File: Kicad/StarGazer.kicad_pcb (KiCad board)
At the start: 4 copper layers, 100 x 100 mm, 102 parts, among them J201 USB_B_Micro, J202 JST - 2x1, J301 JST - 4x1, J302 JST - 4x1, J303 JST - 5x1, J304 JST - 5x1, SW201 JST - 2x1, SW301 RESET PUSH, U101 STM32G070KBT6, U201 STBC08, U202 AP22811BW5-7, U203 TLV75528PDBVR, U301 TSX-3225, U302 LIS3MDLTR, U303 LSM6DS33TR, U304 74HC595PW,112, U305 74HC595PW,112, U306 74HC595PW,112

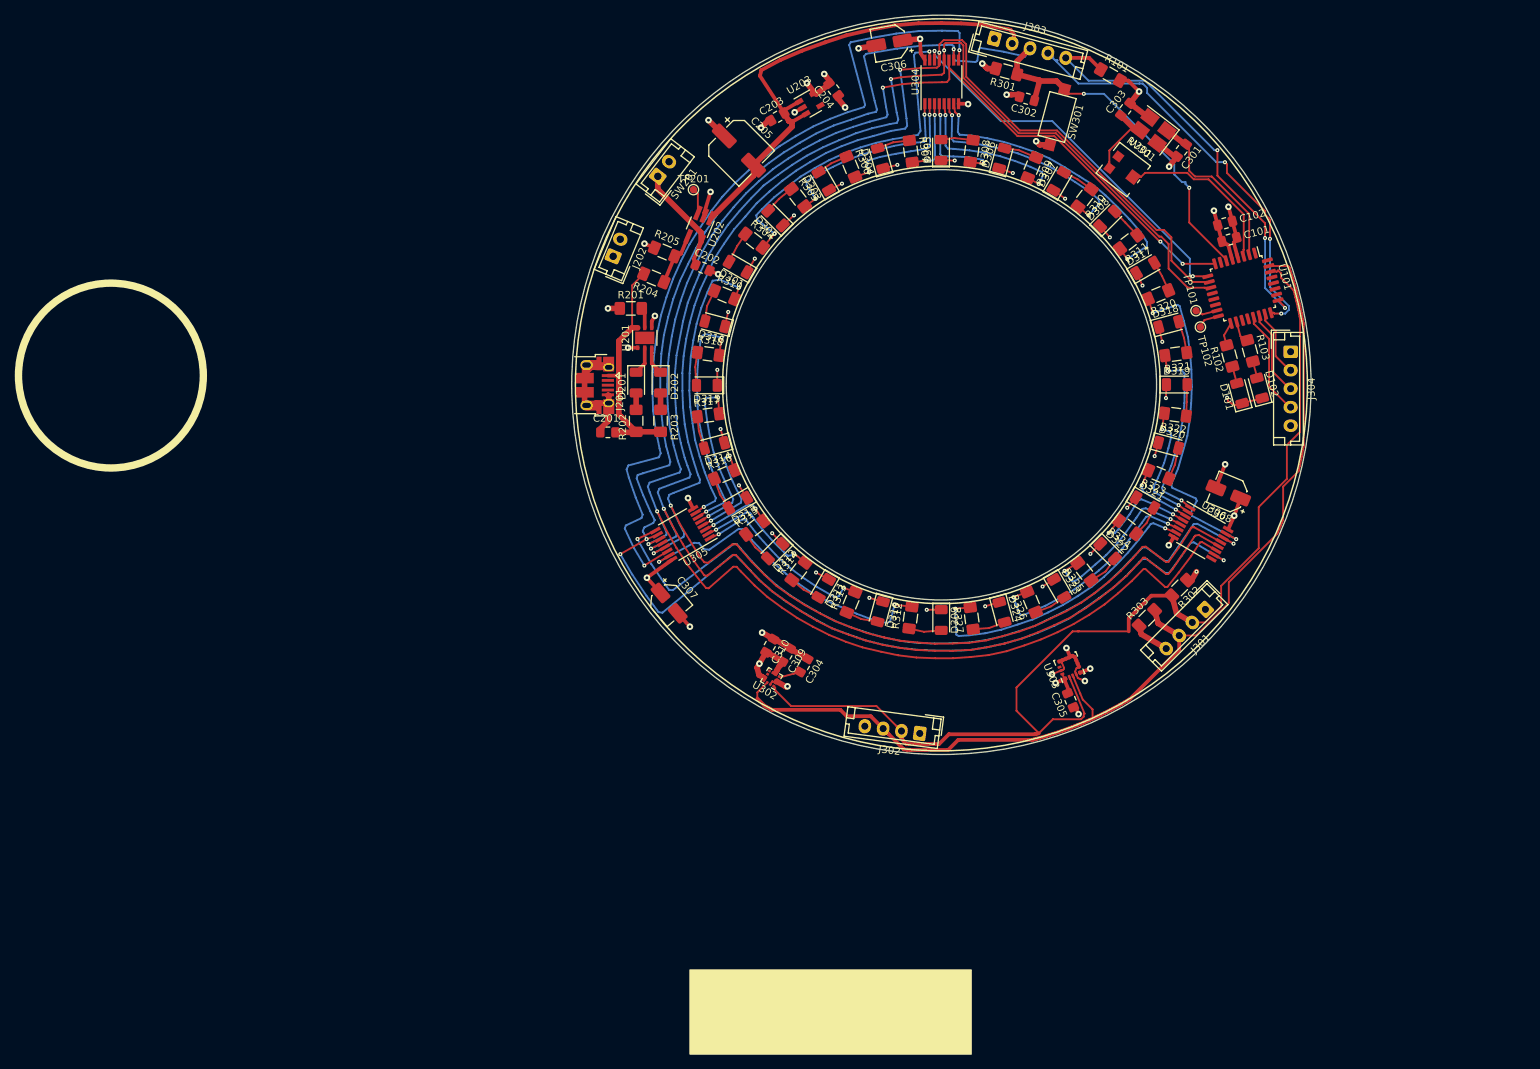
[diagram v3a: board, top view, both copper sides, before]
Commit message: PCB updated to curved traces.  Leftover final polish, screw locations, drill-routing, and art is missing
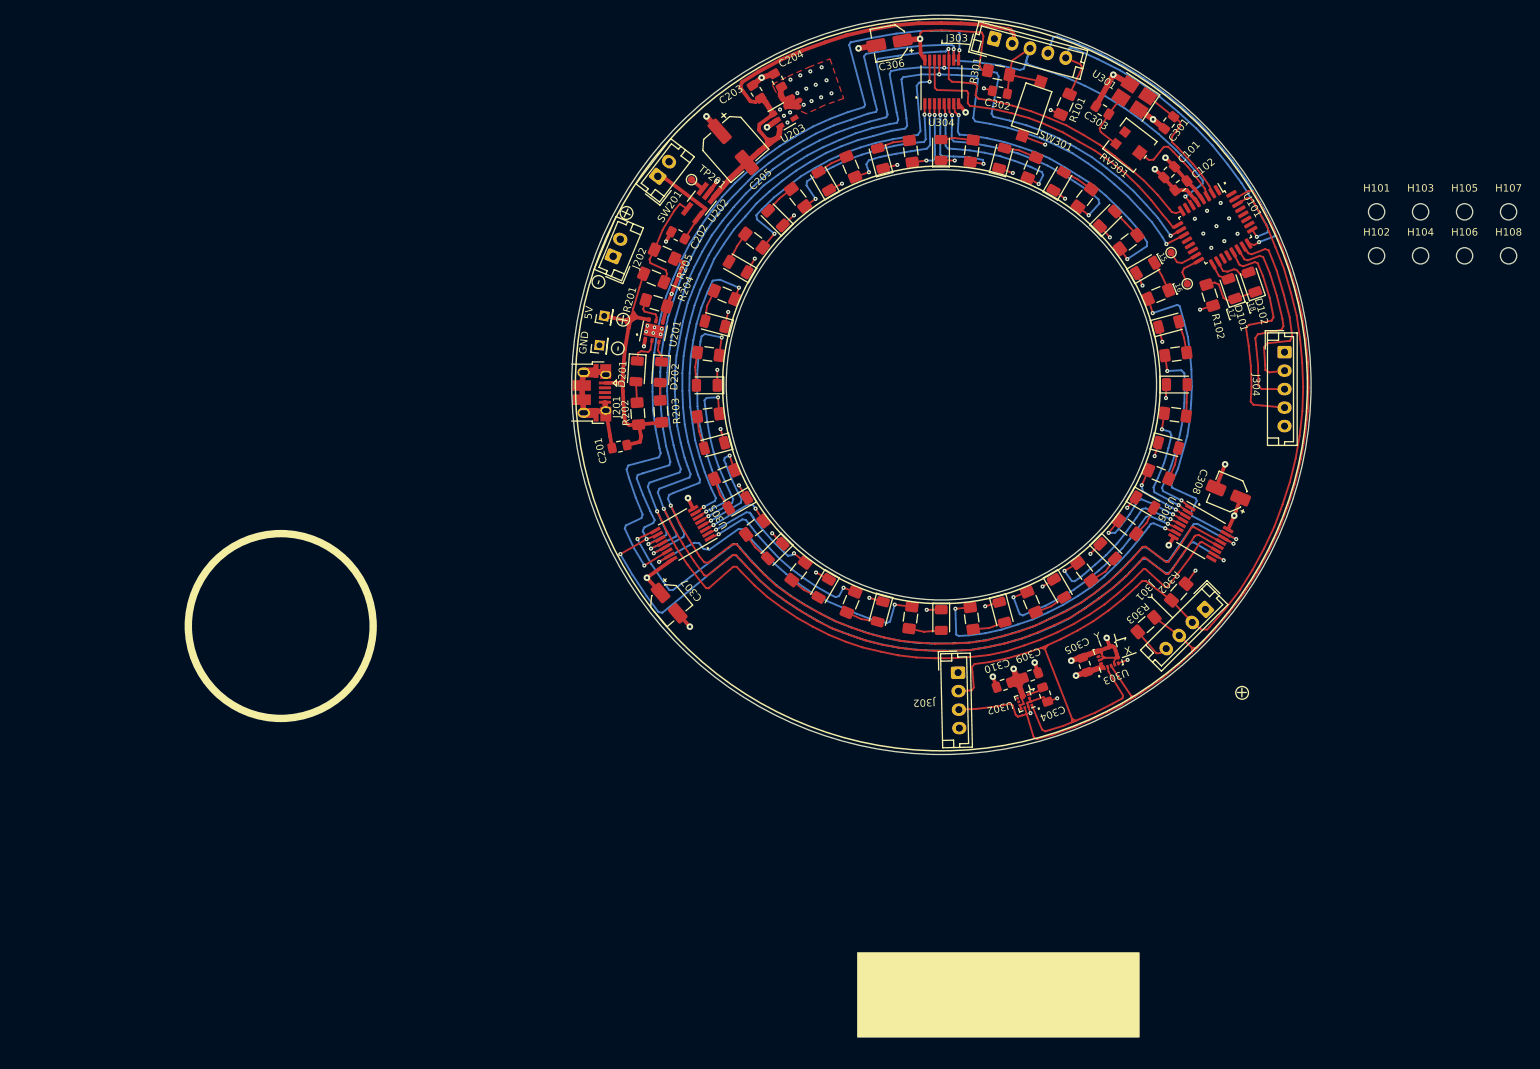
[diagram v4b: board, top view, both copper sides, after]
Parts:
- removed R103: 180ohm, Resistor_SMD:R_1206_3216Metric_Pad1.42x1.75mm_HandSolder
- added H101: MountingHole, MountingHole:MountingHole_2.2mm_M2, F.Cu at (218.8, 66.5)
- added H102: MountingHole, MountingHole:MountingHole_2.2mm_M2, F.Cu at (218.8, 72.5)
- added H103: MountingHole, MountingHole:MountingHole_2.2mm_M2, F.Cu at (224.8, 66.5)
- added H104: MountingHole, MountingHole:MountingHole_2.2mm_M2, F.Cu at (224.8, 72.5)
- added H105: MountingHole, MountingHole:MountingHole_2.2mm_M2, F.Cu at (230.7, 66.5)
- added H106: MountingHole, MountingHole:MountingHole_2.2mm_M2, F.Cu at (230.7, 72.5)
- added H107: MountingHole, MountingHole:MountingHole_2.2mm_M2, F.Cu at (236.7, 66.5)
- added H108: MountingHole, MountingHole:MountingHole_2.2mm_M2, F.Cu at (236.7, 72.5)
- added J203: Conn_01x01, Connector_PinHeader_2.00mm:PinHeader_1x01_P2.00mm_Vertical, F.Cu at (113.7, 84.6)
- added J204: Conn_01x01, Connector_PinHeader_2.00mm:PinHeader_1x01_P2.00mm_Vertical, F.Cu at (114.4, 80.6)
- moved U302 34.4 mm to (171.2, 132.8), turned to 199 degrees
- moved C309 33.2 mm to (172.1, 129.2), turned to 199 degrees
- moved C304 32.9 mm to (174.0, 131.8), turned to 109 degrees
- moved C310 32.1 mm to (168.4, 130.5), turned to 19 degrees
- moved D102 14.4 mm to (202.0, 76.0), turned to 108.8 degrees
- moved D101 14.2 mm to (199.2, 76.9), turned to 108.8 degrees
- moved C101 12.2 mm to (190.8, 61.2), turned to 225.4 degrees
- moved J302 9.71 mm to (162.2, 128.9), turned to 271.3 degrees
- moved U101 9.06 mm to (197.0, 68.6), turned to 300.2 degrees
- moved R102 8.64 mm to (196.3, 77.8), turned to 107.4 degrees
- moved TP101 8.56 mm to (191.0, 72.0)
- moved C102 7.84 mm to (192.4, 63.0), turned to 217.8 degrees
- moved C204 7.65 mm to (137.8, 48.7), turned to 298.5 degrees
- moved R101 7.28 mm to (176.7, 52.0), turned to 246.4 degrees
- moved TP102 6.11 mm to (193.2, 76.3)
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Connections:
- D101 pad 1: GND -> Net-(D101-Pad1)
- D102 pad 1: GND -> Net-(D101-Pad1)
- R102 pad 1: Net-(R102-Pad1) -> GND
- R102 pad 2: Net-(D101-Pad2) -> Net-(D101-Pad1)
- U101 pad 10: SHIFT_REG_OUTPUT_ENABLE_N -> SHIFT_REG_LATCH
- U101 pad 11: SHIFT_REG_LATCH -> SHIFT_REG_OUTPUT_ENABLE_N
- U101 pad 17: Net-(R102-Pad1) -> Net-(D101-Pad2)
- U101 pad 18: Net-(R103-Pad1) -> Net-(D102-Pad2)
- U201 pad 7: (no net) -> GND
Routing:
- net V_REG: track 55.2 -> 74.4 mm, vias 11 -> 20
- net UI_JOY_Y: track 9.07 -> 26.4 mm
- net UI_JOY_X: track 11.7 -> 28.6 mm
- net UI_BUTTON: track 14.3 -> 31.2 mm
- net I2C_SDA: track 141.6 -> 125.2 mm
- net SHIFT_REG_LATCH: track 244.5 -> 232.9 mm
- net SHIFT_REG_OUTPUT_ENABLE_N: track 243.3 -> 231.9 mm
- net V_USB: track 32.1 -> 42.7 mm
- net OSC_OUT: track 23.2 -> 13.6 mm
- net SWDIO: track 57.4 -> 47.9 mm, vias 3 -> 1
- net SWCLK: track 57.6 -> 48.6 mm, vias 3 -> 1
- net I2C_SCL: track 149.9 -> 141.1 mm
- net Net-(D101-Pad1): track 0.00 -> 8.28 mm
- net SHIFT_REG_DATA_IN: track 52.5 -> 44.3 mm, vias 2 -> 0
- net Net-(R204-Pad1): track 7.25 -> 14.3 mm
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- added copper zone on F.Cu, net V_REG
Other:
- board text added: "+"
- board text added: "-"
- board text added: "."
- board text added: "15"
- board text added: "16"
- board text added: "17"
- board text added: "18"
- board text added: "5V"
- board text added: "GND"
- board text added: "X"
- board text added: "Y"

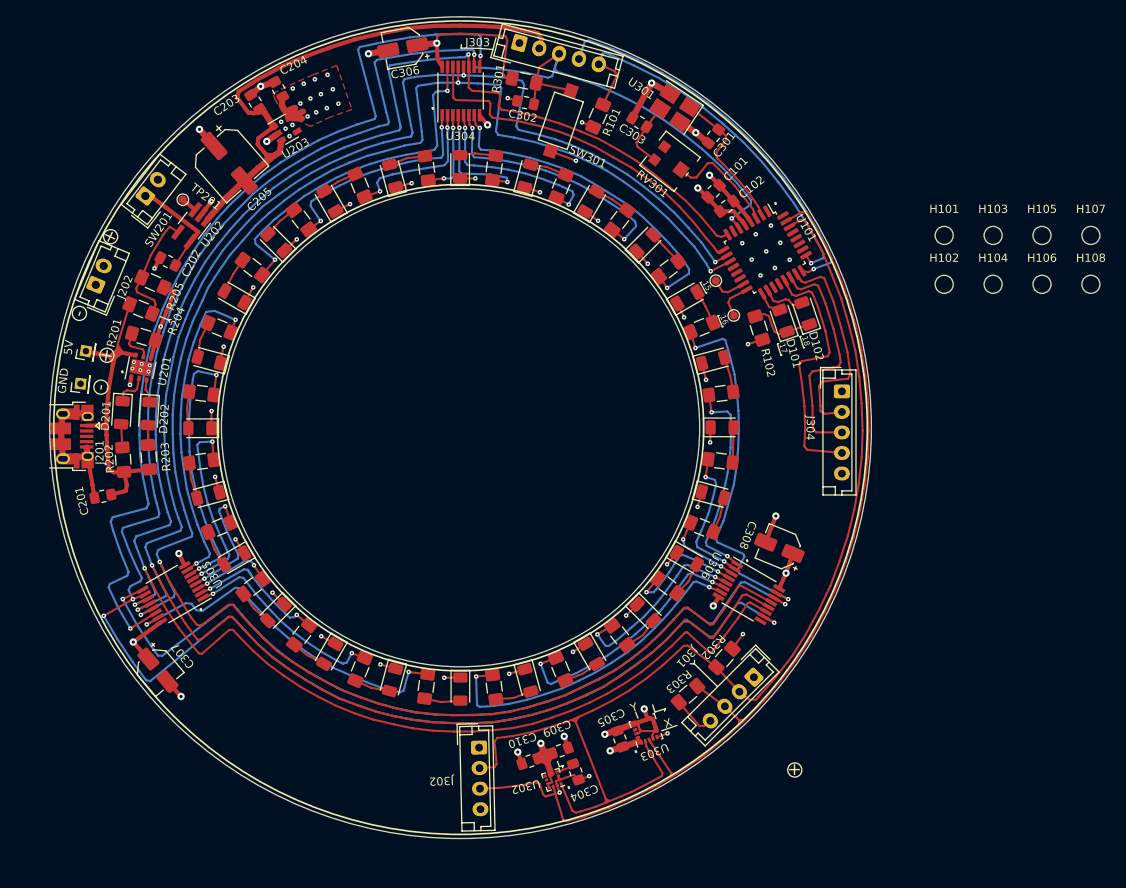
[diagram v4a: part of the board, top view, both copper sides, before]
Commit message: Added screw locations.
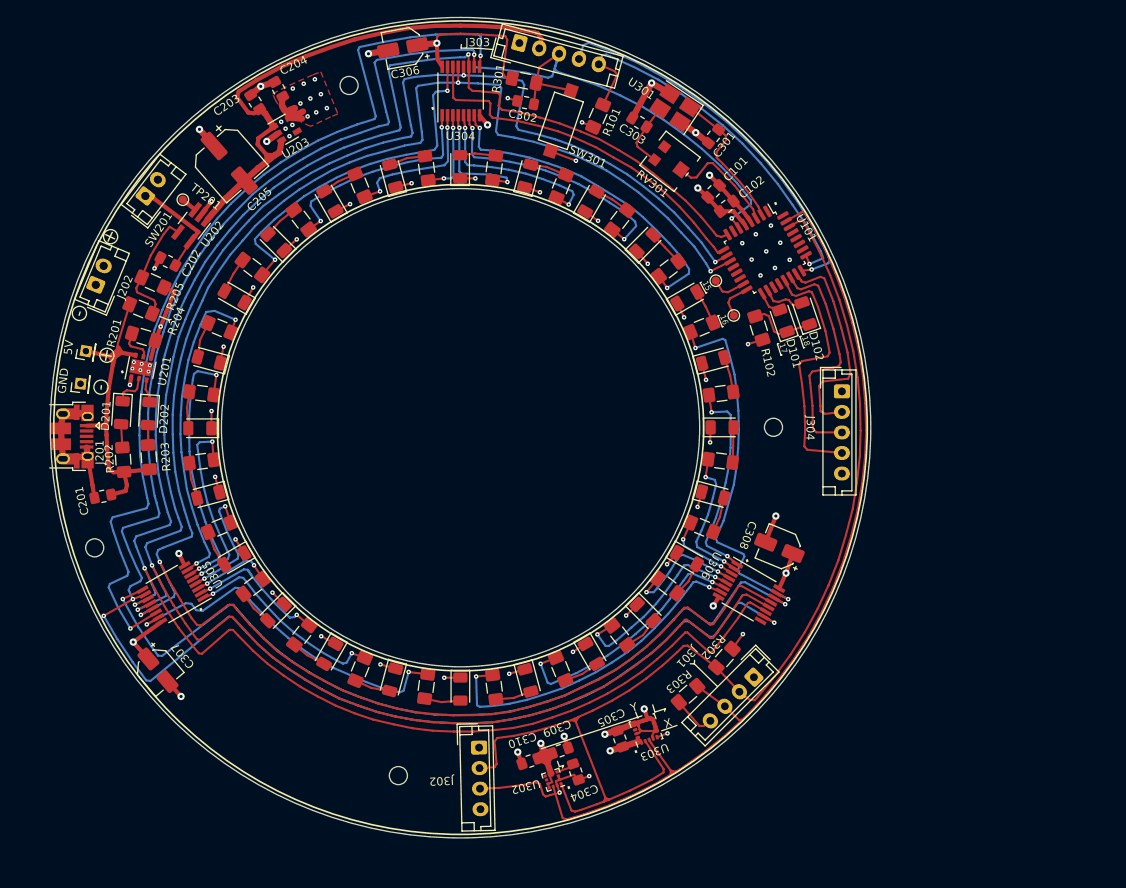
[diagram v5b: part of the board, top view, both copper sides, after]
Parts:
- removed H105, H106, H107, H108: MountingHole, MountingHole:MountingHole_2.2mm_M2
- moved H101 110.2 mm to (115.4, 104.5)
- moved H102 89.4 mm to (152.4, 132.3)
- moved H104 82.0 mm to (146.4, 48.3)
- moved H103 35.5 mm to (198.0, 89.9)
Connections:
- U201 pad 7: GND -> (no net)
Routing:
- net I2C_SDA: track 125.2 -> 122.8 mm
- net SWDIO: track 47.9 -> 46.9 mm
- net I2C_SCL: track 141.1 -> 140.4 mm
- net V_REG: vias 20 -> 17
- net GND: vias 55 -> 49
- net (no net): vias 13 -> 19
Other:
- board size 100 x 100 mm -> 99.9 x 99.9 mm

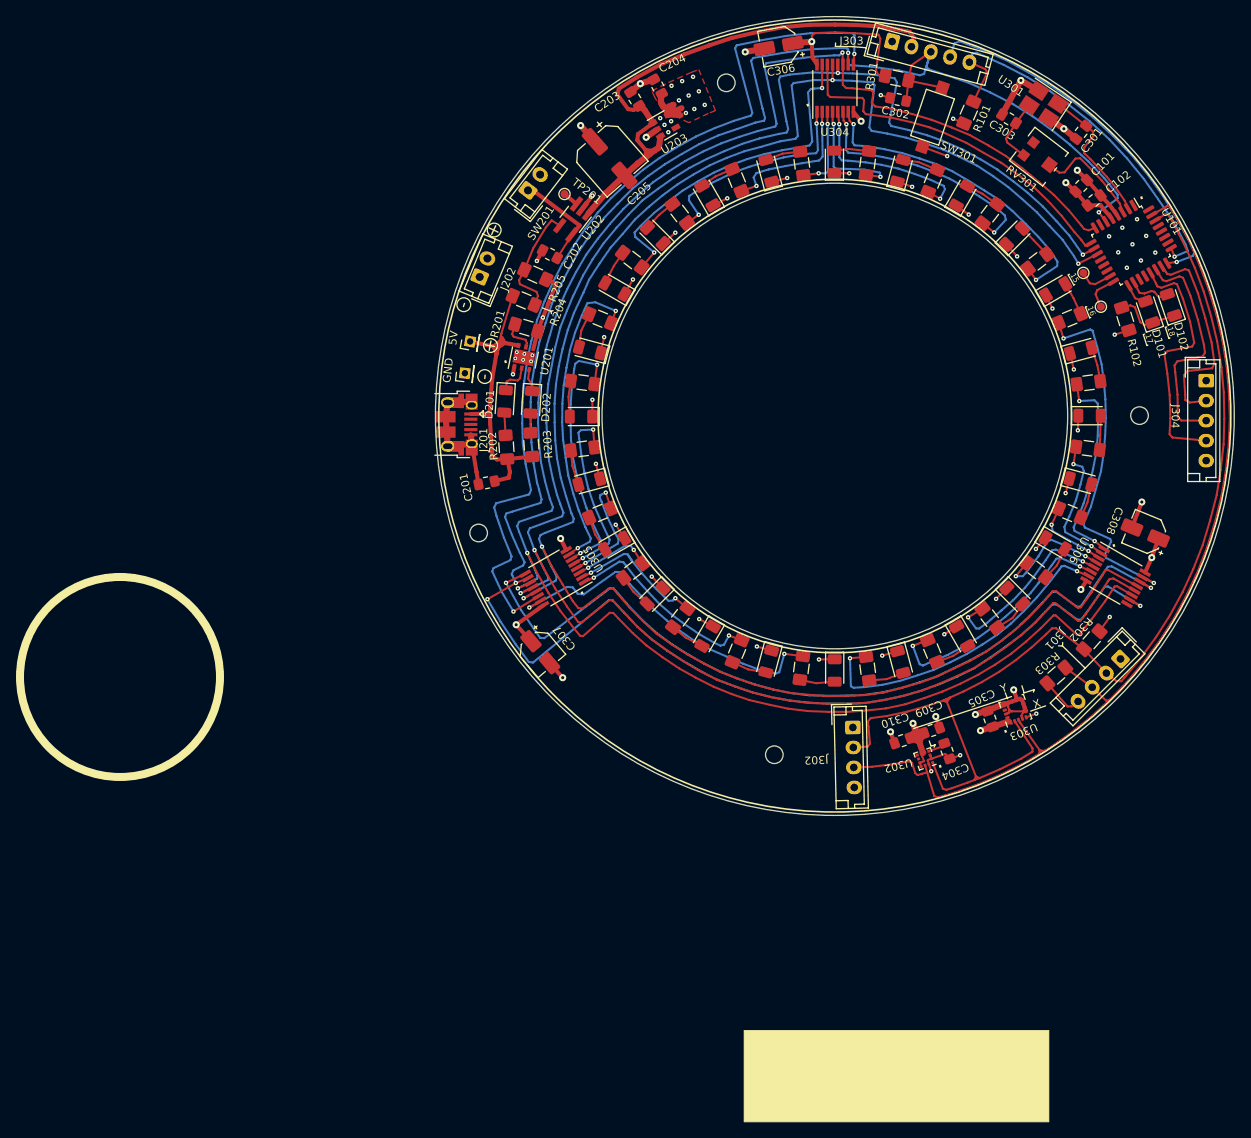
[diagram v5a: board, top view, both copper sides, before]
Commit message: Continued work on PCB.  Added back art.
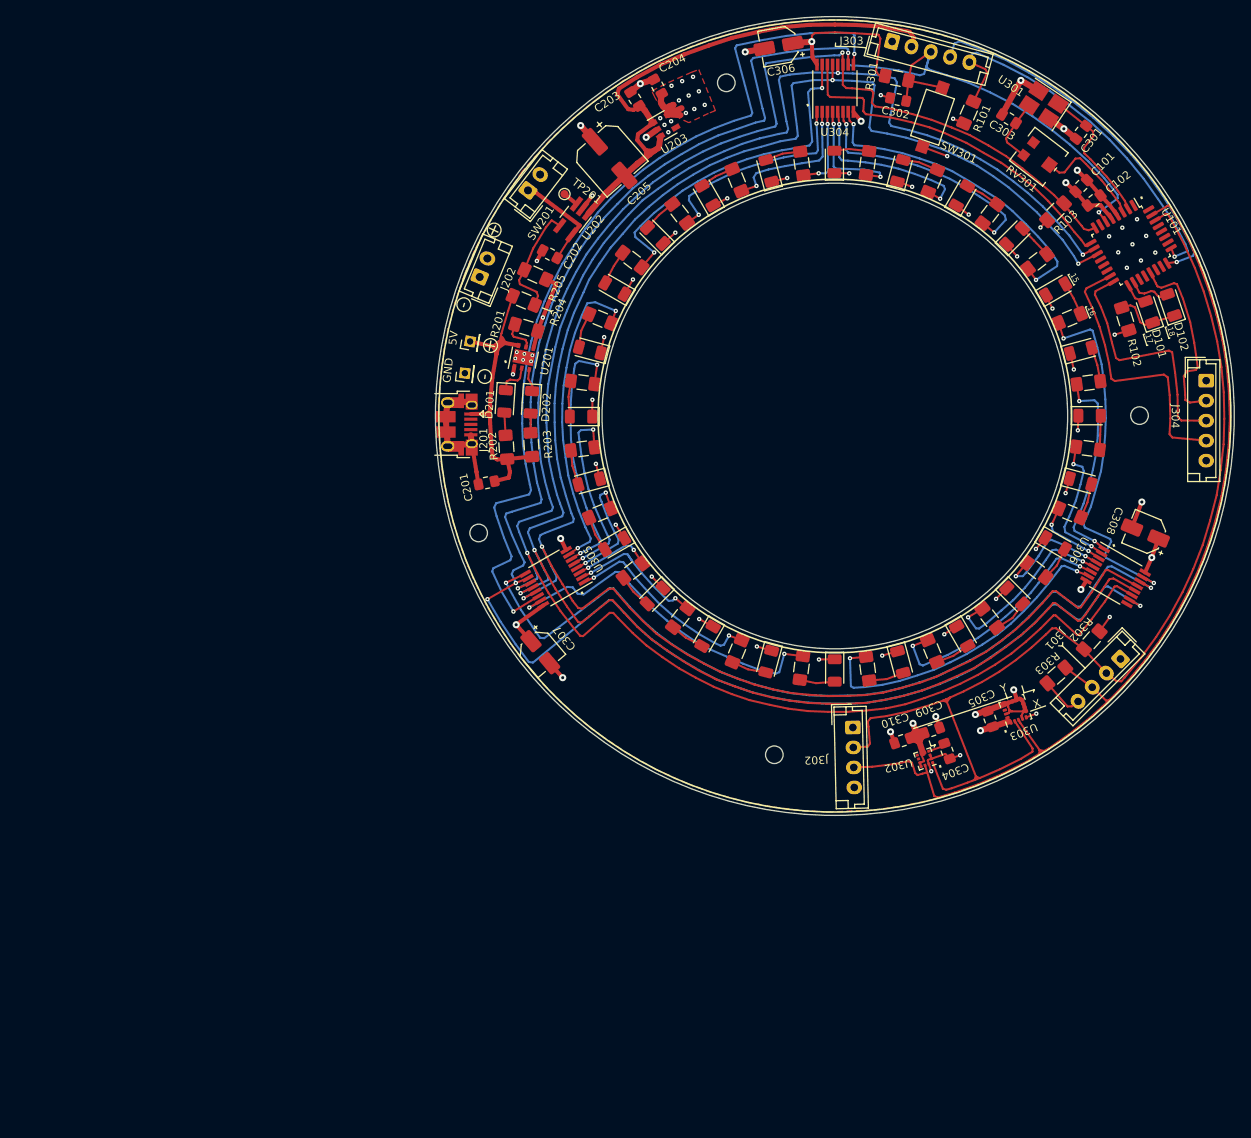
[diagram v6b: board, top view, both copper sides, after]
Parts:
- removed TP101, TP102: Connector_TestPoint, TestPoint:TestPoint_Pad_D1.0mm
- added G***: LOGO, Kicad:Test_Background, B.Cu at (160.0, 89.9)
- added R103: 10kohm, Resistor_SMD:R_1206_3216Metric_Pad1.42x1.75mm_HandSolder, F.Cu at (187.5, 64.4)
- R302, R303: value R_I2C_PULLUP -> 10kohm
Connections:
- J304 pad 2: UI_JOY_Y -> UI_BUTTON
- J304 pad 4: UI_BUTTON -> UI_JOY_Y
- U101 pad 15: Net-(TP101-Pad1) -> UI_JOY_Y
- U101 pad 16: Net-(TP102-Pad1) -> UI_JOY_X
- U101 pad 22: UI_JOY_X -> (no net)
- U101 pad 23: UI_JOY_Y -> (no net)
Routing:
- net UI_JOY_Y: track 26.4 -> 34.5 mm
- net UI_BUTTON: track 31.2 -> 23.2 mm
- net Net-(TP102-Pad1): track 4.54 -> 0.00 mm
- net Net-(TP101-Pad1): track 4.34 -> 0.00 mm
- net UI_JOY_X: track 28.6 -> 30.5 mm
- net GND: track 153.1 -> 154.4 mm, vias 49 -> 50
- added copper zone on B.Cu, net GND
- added copper zone on F.Cu, net GND
